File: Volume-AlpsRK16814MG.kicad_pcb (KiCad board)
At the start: 2 copper layers, 62.9 x 32.4 mm, 10 parts, among them P1 AB I/O, P2 CD I/O, P3 PWR, P4 CTRL, P5 GND, U1 SN754410

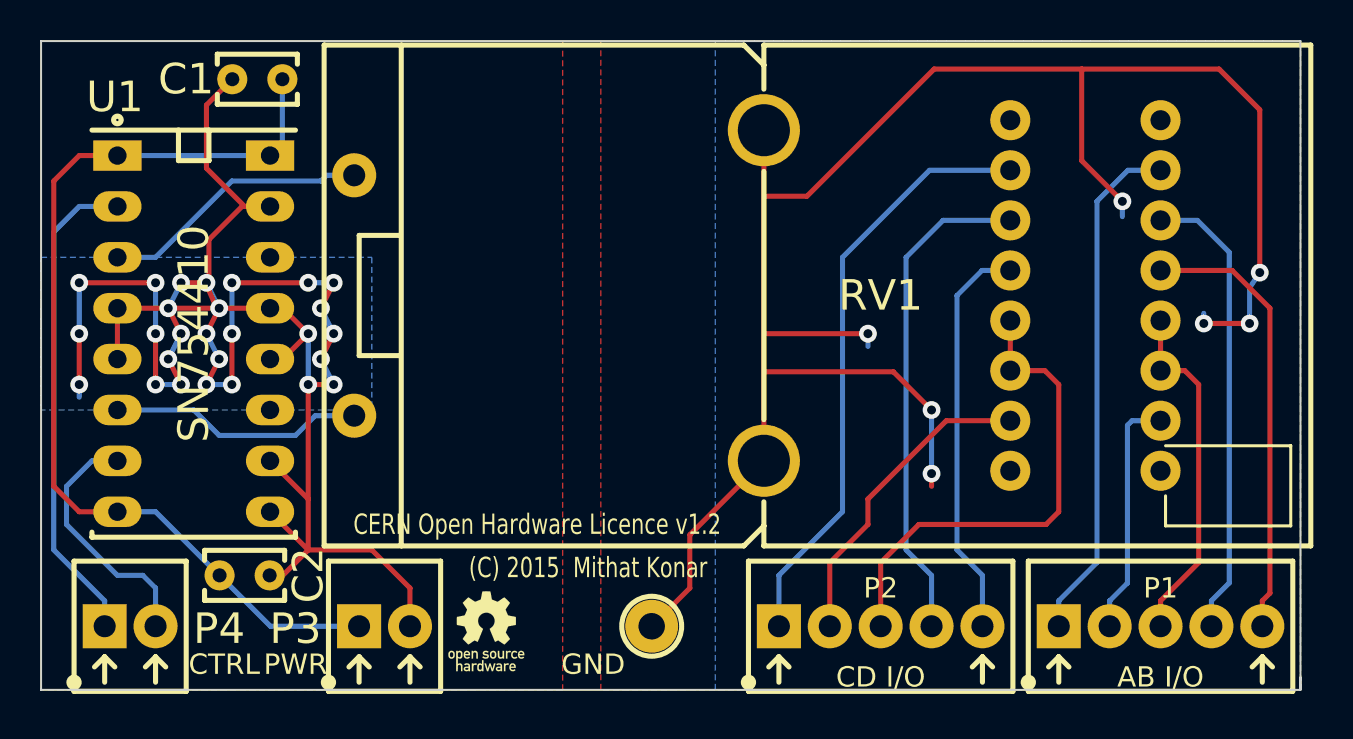
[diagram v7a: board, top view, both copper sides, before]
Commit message: Added jumper to connect motor and digital supplies to schematic; PCB updated.
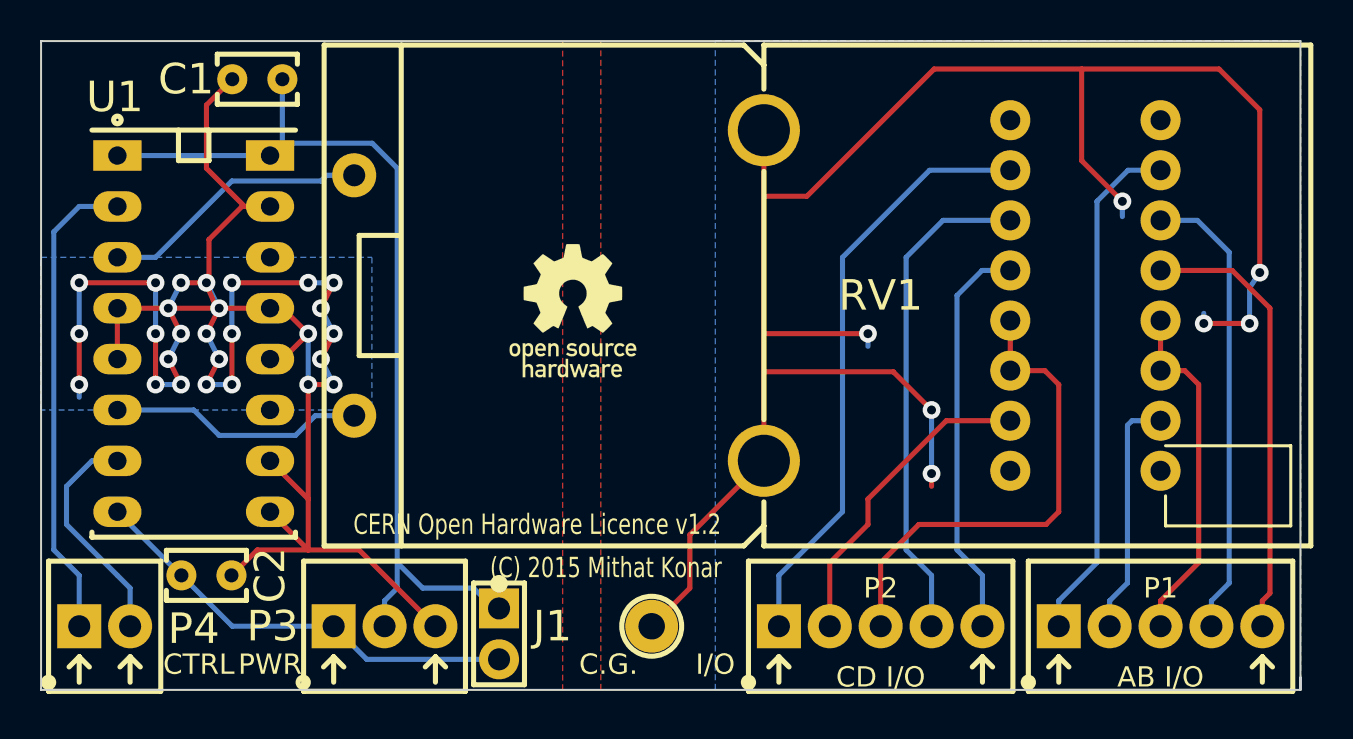
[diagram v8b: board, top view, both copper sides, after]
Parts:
- removed the VAL at (135.9, 116.5)
- added J1: PWR_BR, mfk-SIL-2, F.Cu at (136.5, 116.6)
- added VAL: REF, oshw-logo-250mil-FSilk, F.Cu at (140.2, 100.5)
- added VAL: REF, oshw-logo-notext-100mil-FSilk, B.Cu at (145.9, 93.9)
- P3: footprint mfk-TE_282834-2 -> mfk-TE_282834-3
- P5: value GND -> C.G.
- moved C2 1.91 mm to (121.9, 113.7)
- moved P4 1.27 mm to (116.8, 116.2)
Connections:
- C2 pad 1: +5VD -> /V_MOT
- P3 pad 1: +5VD -> /V_MOT
- P3 pad 2: DGND -> +5VD
- U1 pad 8: +5VD -> /V_MOT
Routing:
- net /V_MOT: track 0.00 -> 22.1 mm
- net DGND: track 102.0 -> 104.7 mm
- net /VOL_DOWN: track 12.6 -> 11.4 mm
- net +5VD: track 48.8 -> 48.0 mm
- net /VOL_UP: track 24.4 -> 23.9 mm
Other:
- board text added: "Copyright (C) 2015 Mithat Konar"
- board text added: "I/O"
- board text added: "V_MOT"
- board text added: "Volume-AlpsRK16814MG v1.0"
